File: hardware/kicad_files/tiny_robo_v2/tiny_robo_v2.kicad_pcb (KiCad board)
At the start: 2 copper layers, 25.4 x 39.1 mm, 31 parts, among them P1 CONN_01X06, P2 BATT, P3 CONN_01X02, P4 CONNECTOR, P5 CONNECTOR, P6 CONN_01X02, SW1 SPDT, U1 MCP73831, U2 MIC5265, U3 ESP8266-ESP-03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

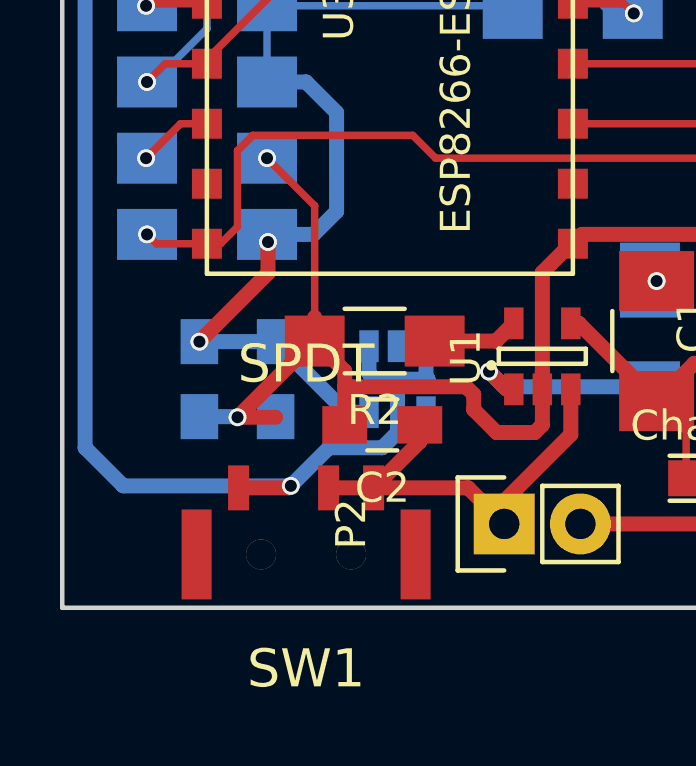
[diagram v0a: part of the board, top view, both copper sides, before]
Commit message: Fixed regulator grounding error, added debug LED on GPIO2
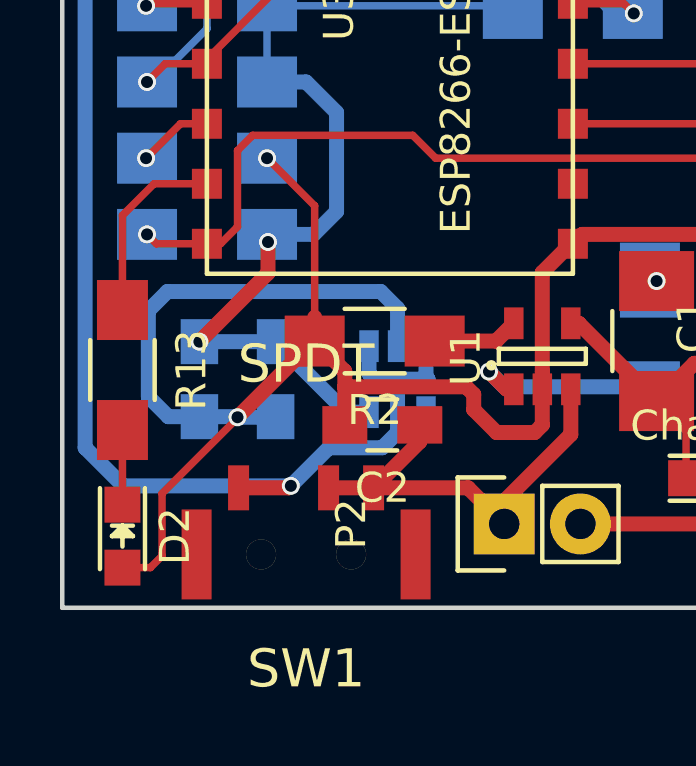
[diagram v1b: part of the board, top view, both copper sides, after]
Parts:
- added D2: LED, LEDs:LED_0805, F.Cu at (159.5, 111.7)
- added R13: 1k, Resistors_SMD:R_1206_HandSoldering, F.Cu at (159.5, 106.1)
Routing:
- net GND: track 103.5 -> 125.5 mm
- net Net-(R13-Pad1): track 0.00 -> 6.41 mm
- net Net-(D2-Pad1): track 0.00 -> 2.49 mm

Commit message: Updated schematic, board probably needs relayout (after I graduate).
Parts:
- removed D2: LED, LEDs:LED_0805
- removed R13: 1k, Resistors_SMD:R_1206_HandSoldering
- added C5: 0.1uF, Capacitors_SMD:C_0805_HandSoldering, F.Cu at (159.5, 110.7)
- added C6: 0.1uF, Capacitors_SMD:C_0805_HandSoldering, F.Cu at (179.3, 112.8)
- added J1: Conn_01x01, Pin_Headers:Pin_Header_Straight_1x01_Pitch1.00mm, F.Cu at (159.5, 106.2)
- P2: value BATT -> CONNECTOR
- P3: value CONN_01X02 -> CONNECTOR
- P4: value CONNECTOR -> BATT
- P5: value CONNECTOR -> CONN_01X02
- R1: value 470 -> 10k
- R10, R11: value 10k -> 1k
- R2: value 2k -> 470
- R3: value 0.22 -> 10k
- R4: value 0.22 -> 2k
- R6: value 1k -> 10k
- R7: value 1k -> 0.22
- R8: value 10k -> 0.22
- U2: value MIC5265 -> ESP8266-ESP-03
- U3: value ESP8266-ESP-03 -> MIC5265
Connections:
- P2 pad 1: +BATT -> GND
- P2 pad 2: GND -> (no net)
- P3 pad 1: Net-(P3-Pad1) -> GND
- P3 pad 2: Net-(P3-Pad2) -> (no net)
- P4 pad 1: GND -> +BATT
- P5 pad 1: GND -> Net-(P5-Pad1)
- R1 pad 1: Net-(Charge1-Pad2) -> +3.3V
- R1 pad 2: Net-(R1-Pad2) -> Net-(P1-Pad1)
- R10 pad 2: Net-(P1-Pad1) -> SCL
- R11 pad 2: Net-(P1-Pad5) -> SDA
- R12 pad 1: GND -> +3.3V
- R12 pad 2: Net-(R12-Pad2) -> Fault2
- R2 pad 1: Net-(R2-Pad1) -> Net-(Charge1-Pad2)
- R2 pad 2: GND -> Net-(R2-Pad2)
- R3 pad 1: Net-(R3-Pad1) -> +3.3V
- R3 pad 2: GND -> Net-(P1-Pad5)
- R5 pad 2: Net-(R5-Pad2) -> Net-(J1-Pad1)
- R6 pad 1: +3.3V -> GND
- R6 pad 2: SCL -> Net-(R6-Pad2)
- R7 pad 1: +3.3V -> Net-(R7-Pad1)
- R7 pad 2: SDA -> GND
- R8 pad 1: +3.3V -> Net-(R8-Pad1)
- R8 pad 2: Fault2 -> GND
- R9 pad 2: Fault1 -> Net-(R9-Pad2)
- U1 pad 1: Net-(R1-Pad2) -> Net-(R2-Pad2)
- U1 pad 5: Net-(R2-Pad1) -> Net-(R4-Pad1)
- U2 pad 1: Unreg -> GND
- U2 pad 2: GND -> (no net)
- U2 pad 3: Unreg -> Net-(P1-Pad2)
- U2 pad 4: Net-(U2-Pad4) -> Net-(P1-Pad3)
- U2 pad 5: +3.3V -> Fault1
- U3 pad 1: GND -> Unreg
- U3 pad 10: SCL -> (no net)
- U3 pad 11: SDA -> (no net)
- U3 pad 12: Net-(R12-Pad2) -> (no net)
- U3 pad 13: Net-(R13-Pad1) -> (no net)
- U3 pad 14: Net-(P1-Pad1) -> (no net)
- U3 pad 2: (no net) -> GND
- U3 pad 3: Net-(P1-Pad2) -> Unreg
- U3 pad 4: Net-(P1-Pad3) -> Net-(U3-Pad4)
- U3 pad 5: Fault1 -> +3.3V
- U3 pad 6: Net-(P1-Pad5) -> (no net)
- U3 pad 7: Net-(U3-Pad7) -> (no net)
- U3 pad 8: +3.3V -> (no net)
- U3 pad 9: Fault2 -> (no net)
- U4 pad 1: Net-(P3-Pad2) -> Net-(P5-Pad2)
- U4 pad 2: Net-(R3-Pad1) -> Net-(R7-Pad1)
- U4 pad 3: Net-(P3-Pad1) -> Net-(P5-Pad1)
- U4 pad 7: Net-(R5-Pad2) -> Net-(R9-Pad2)
- U4 pad 8: Net-(R5-Pad2) -> Net-(R9-Pad2)
- U5 pad 2: Net-(R4-Pad1) -> Net-(R8-Pad1)
- U5 pad 8: Net-(R5-Pad2) -> Net-(R9-Pad2)
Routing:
- net GND: track 125.5 -> 204.7 mm, vias 2 -> 6
- net Unreg: track 83.9 -> 22.7 mm, vias 1 -> 0
- net SDA: track 29.7 -> 6.34 mm, vias 2 -> 1
- net Net-(R5-Pad2): track 19.1 -> 0.00 mm, vias 2 -> 0
- net Net-(J1-Pad1): track 0.00 -> 14.6 mm, vias 0 -> 2
- net Net-(R2-Pad2): track 0.00 -> 11.4 mm
- net Net-(P5-Pad1): track 0.00 -> 9.63 mm
- net Net-(R9-Pad2): track 0.00 -> 7.84 mm, vias 0 -> 1
- net Net-(R1-Pad2): track 6.65 -> 0.00 mm, vias 1 -> 0
- net Fault2: track 10.3 -> 3.85 mm, vias 2 -> 1
- net Net-(R13-Pad1): track 6.41 -> 0.00 mm
- net Net-(R3-Pad1): track 6.28 -> 0.00 mm, vias 2 -> 0
- net Net-(P1-Pad1): track 23.8 -> 29.4 mm
- net Net-(P5-Pad2): track 0.00 -> 4.70 mm
- net Net-(P3-Pad2): track 4.70 -> 0.00 mm
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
